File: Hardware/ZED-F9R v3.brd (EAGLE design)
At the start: 43.2 x 50.8 mm, 152 parts, among them J3 QWIIC_RIGHT_ANGLE, J4 QWIIC_RIGHT_ANGLE, U1 DUAL-OPTO_HCPL-073LSOIC-8, U2 U-BLOX_ZED_F9R, U3 UHS_INVERTER_SCHMITT_TRIGGERS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, U4 UHS_INVERTER_SCHMITT_TRIGGERS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, U5 3.3V

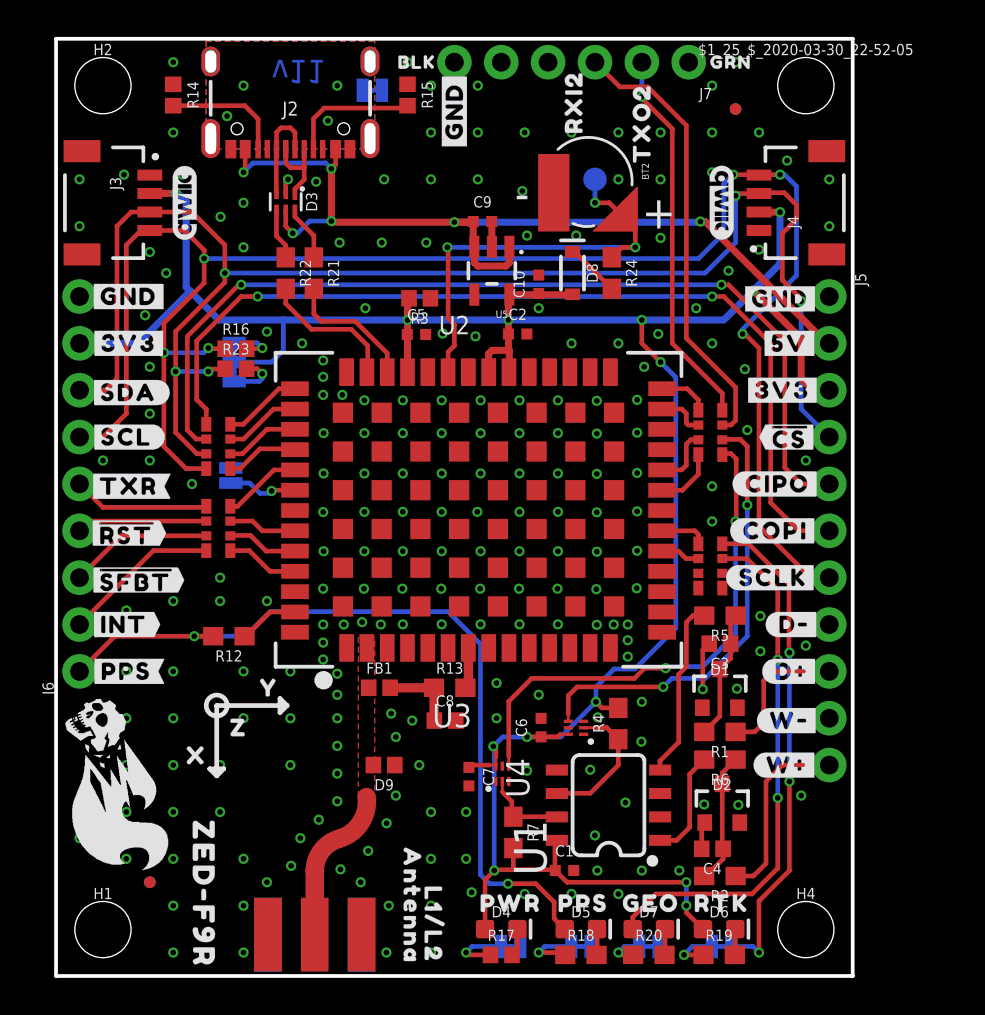
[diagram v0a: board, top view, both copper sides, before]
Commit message: Adds more capacitance to power lines
* Fixes various trace irregularities
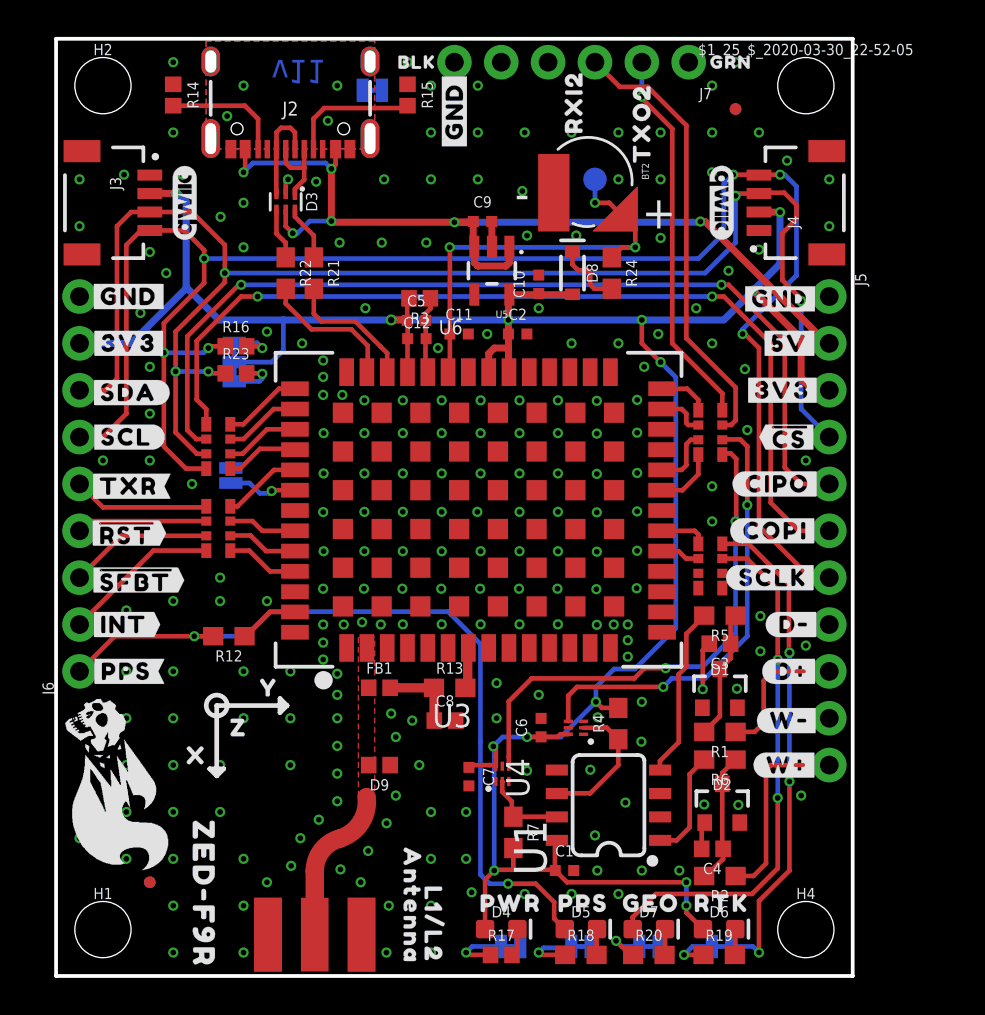
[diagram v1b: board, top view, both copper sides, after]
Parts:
- added C11: 2.2uF, SparkFun-Capacitors:0402-TIGHT
- added C12: 0.1uF, SparkFun-Capacitors:0402-TIGHT
- R18, R19, R20: value 4.7k -> 2.2k
- U6: value U-BLOX_ZED_F9R -> U-BLOX_ZED-F9R
- moved C5 0.76 mm to (19.5, 35.5)
- moved D9 0.25 mm to (17.5, 11.4)
- moved R23 0.25 mm to (9.75, 32.7)
- moved R16 0.13 mm to (9.75, 34.1)
- renumbered U2 to U6
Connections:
- net 3.3V: now also C12.1
- net GND: now also C11.2, C12.2
- net V_BATT: now also C11.1
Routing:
- net GND: track 6.31 -> 10.5 mm
- net 3.3V: track 141.7 -> 143.3 mm
- net N$2: track 2.96 -> 3.74 mm
- net DIR_INV: track 7.52 -> 8.14 mm
- net N$33: track 2.12 -> 2.63 mm
